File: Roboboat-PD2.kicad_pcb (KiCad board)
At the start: 2 copper layers, 78 x 81.5 mm, 38 parts, among them J1 14.4V, J10 Motor, J11 Motor, J12 Motor, J13 Motor, J14 Motor, J15 Motor, J16 Motor, J17 GND TP, J2 PGOOD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

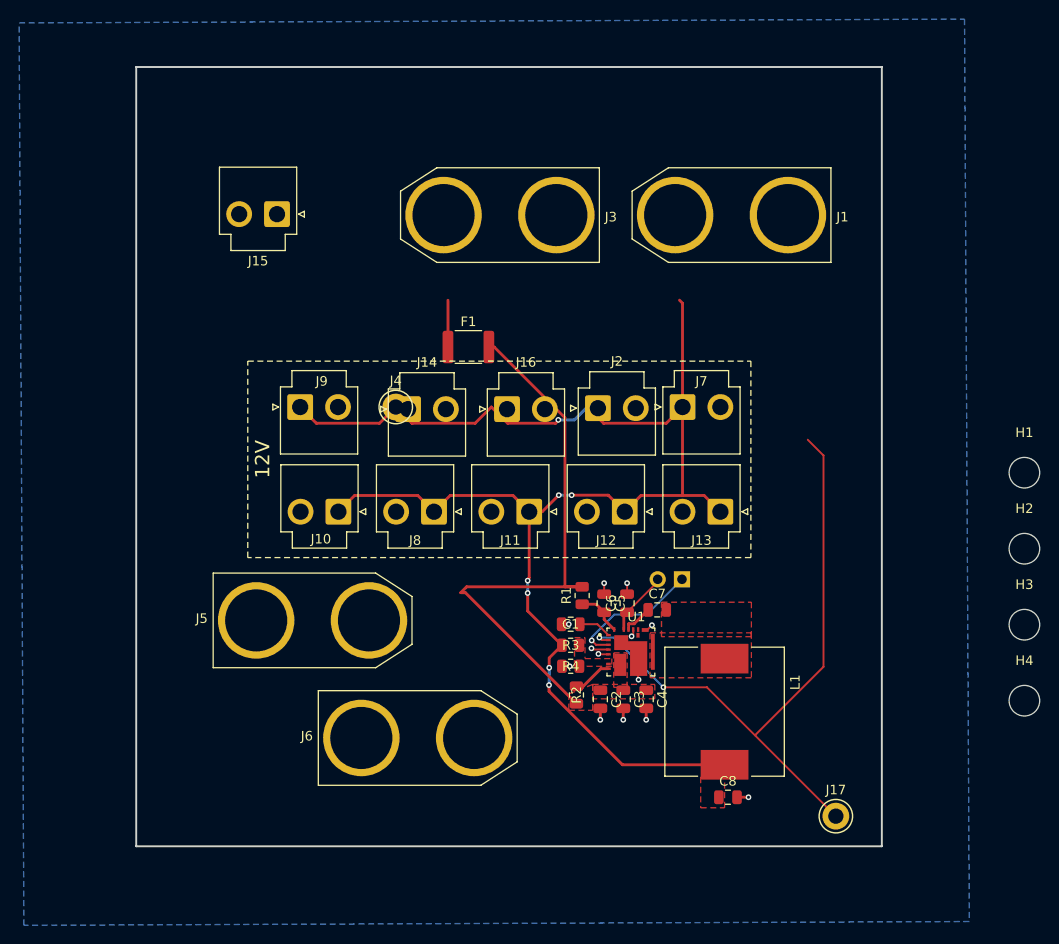
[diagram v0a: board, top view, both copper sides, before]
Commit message: add 0.1uF capacitors to PGOOD output
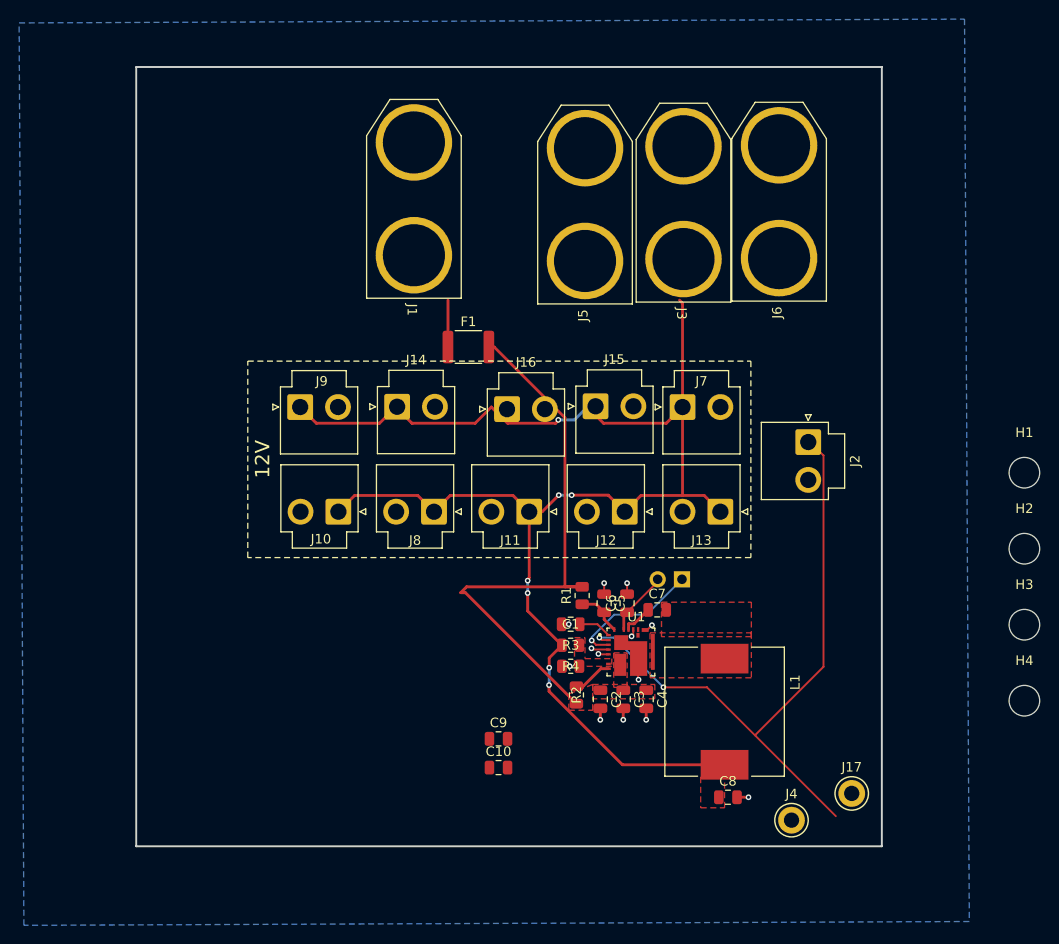
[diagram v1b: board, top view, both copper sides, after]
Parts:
- added C10: 0.1uF, Capacitor_SMD:C_0805_2012Metric, F.Cu at (133.6, 130.7)
- added C9: 0.1uF, Capacitor_SMD:C_0805_2012Metric, F.Cu at (133.6, 127.7)
- moved J6 67.6 mm to (162.9, 71.5), turned to 90 degrees
- moved J4 59.8 mm to (164.2, 136.2)
- moved J5 52.0 mm to (142.6, 71.8), turned to 90 degrees
- moved J15 38.9 mm to (143.7, 92.9), turned to 0 degrees
- moved J1 33.3 mm to (124.7, 71.2), turned to 90 degrees
- moved J2 22.3 mm to (165.9, 96.6), turned to -90 degrees
- moved J3 19.2 mm to (152.9, 71.6), turned to 90 degrees
- moved J17 2.90 mm to (170.5, 133.4)
- moved J14 1.17 mm to (122.9, 93.0)
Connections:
- J17 pad 1: GND -> Net-(J17-Pin_1)
- J2 pad 2: GND -> Net-(J2-Pin_2)

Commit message: add 0.1uF capacitors to PGOOD output
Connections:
- C10 pad 1: Net-(J17-Pin_1) -> /PGOOD
- C9 pad 1: Net-(J2-Pin_2) -> /PGOOD
- J17 pad 1: Net-(J17-Pin_1) -> GND
- J2 pad 2: Net-(J2-Pin_2) -> /PGOOD
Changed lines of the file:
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@@
 	(net 13 "Net-(SW1-A)")
 	(net 14 "Net-(SW1-B)")
-	(net 15 "Net-(J2-Pin_2)")
-	(net 16 "Net-(J17-Pin_1)")
 	(footprint "Capacitor_SMD:C_0805_2012Metric"
 		(layer "F.Cu")
@@
 			(layers "*.Cu" "*.Mask")
 			(remove_unused_layers no)
-			(net 16 "Net-(J17-Pin_1)")
+			(net 1 "GND")
 			(pinfunction "Pin_1")
 			(pintype "passive")
@@
 			(layers "*.Cu" "*.Mask")
 			(remove_unused_layers no)
-			(net 15 "Net-(J2-Pin_2)")
+			(net 3 "/PGOOD")
 			(pinfunction "Pin_2")
 			(pintype "passive")
@@
 			(layers "F.Cu" "F.Paste" "F.Mask")
 			(roundrect_rratio 0.25)
-			(net 15 "Net-(J2-Pin_2)")
+			(net 3 "/PGOOD")
 			(pintype "passive")
 		)
@@
 			(layers "F.Cu" "F.Paste" "F.Mask")
 			(roundrect_rratio 0.25)
-			(net 16 "Net-(J17-Pin_1)")
+			(net 3 "/PGOOD")
 			(pintype "passive")
 		)
@@
 		(tags "connector JST VH vertical")
 		(property "Reference" "J15"
-			(at 1.98 -4.9 360)
+			(at 1.98 -4.9 0)
 			(layer "F.SilkS")
 			(effects
@@
 		)
 		(property "Value" "Motor"
-			(at 1.98 6 360)
+			(at 1.98 6 0)
 			(layer "F.Fab")
 			(effects
@@
 		)
 		(fp_text user "${REFERENCE}"
-			(at 1.98 4.1 360)
+			(at 1.98 4.1 0)
 			(layer "F.Fab")
 			(effects

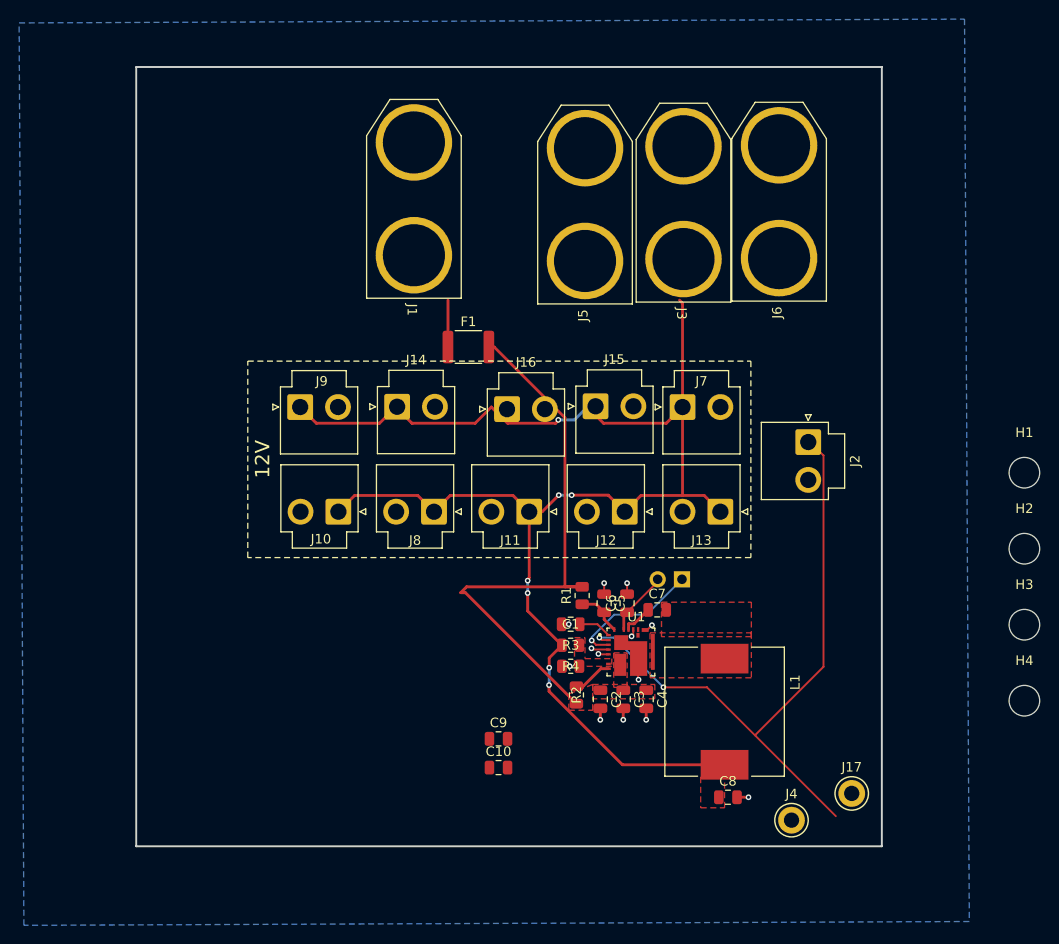
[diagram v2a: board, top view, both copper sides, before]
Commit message: redo PCB layout
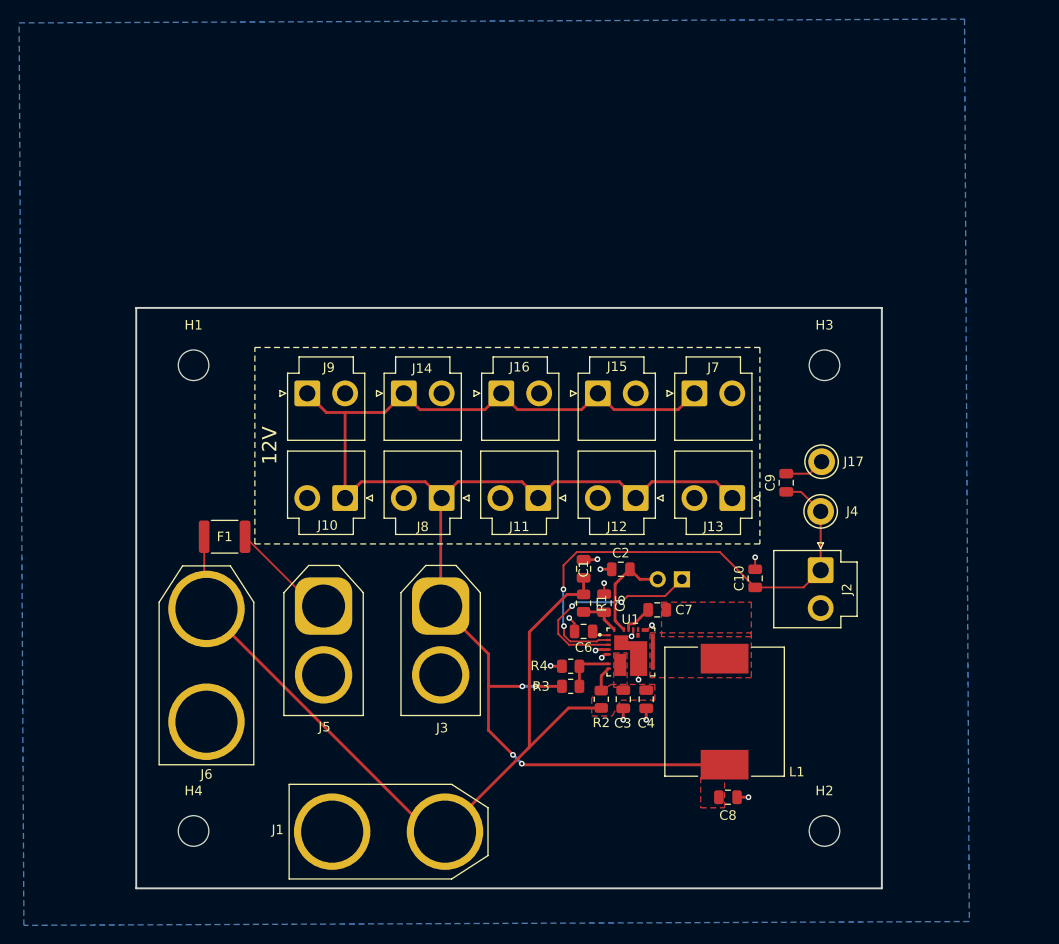
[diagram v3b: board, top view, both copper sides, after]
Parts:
- J3, J5: footprint footprints:XT90_V -> Connector_AMASS:AMASS_XT60-M_1x02_P7.20mm_Vertical
- moved H4 88.0 mm to (101.7, 137.3)
- moved H1 87.6 mm to (101.7, 88.6)
- moved J6 77.1 mm to (103.0, 120.0)
- moved J1 66.3 mm to (122.0, 137.4), turned to 0 degrees
- moved J5 50.1 mm to (115.2, 113.8), turned to -90 degrees
- moved J3 49.3 mm to (127.5, 113.8), turned to -90 degrees
- moved C9 40.3 mm to (163.7, 100.9), turned to 90 degrees
- moved H2 36.2 mm to (167.7, 137.3)
- moved J17 34.8 mm to (167.3, 98.7)
- moved H3 34.3 mm to (167.7, 88.6)
- moved C10 33.4 mm to (160.4, 110.9), turned to 90 degrees
- moved J4 32.4 mm to (167.2, 103.9)
- moved F1 32.3 mm to (104.9, 106.5), turned to 180 degrees
- moved C2 13.8 mm to (146.3, 110.0), turned to 180 degrees
- moved J2 13.5 mm to (167.2, 110.0)
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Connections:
- J2 pad 2: /PGOOD -> GND
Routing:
- net +14.4V: track 60.4 -> 83.2 mm
- net /PGOOD: track 68.1 -> 52.7 mm
- net Net-(SW1-A): track 14.2 -> 21.9 mm, vias 1 -> 2
- net +12V: track 154.3 -> 161.7 mm, vias 7 -> 4
- net GND: track 15.5 -> 21.7 mm, vias 13 -> 14
- net Net-(J5-Pin_1): track 4.89 -> 10.3 mm
- net Net-(U1-FB): track 0.00 -> 4.89 mm
- net Net-(SW1-B): track 5.99 -> 10.7 mm
- net Net-(U1-SS): track 3.48 -> 1.82 mm
- net Net-(U1-TON): track 4.11 -> 2.60 mm
- removed copper zone on F.Cu, net Net-(U1-FB)
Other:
- board size 78 x 81.5 mm -> 78 x 60.7 mm

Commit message: better silkscreens
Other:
- board text added: "14.4V"
- board text added: "14.4V INPUT"
- board text added: "FUSED 14.4V"
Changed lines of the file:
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@@
 		)
 		(property "Footprint" "footprints:XT90_V"
-			(at 0 0 360)
+			(at 0 0 0)
 			(layer "F.Fab")
 			(hide yes)
@@
 		)
 		(property "Datasheet" ""
-			(at 0 0 360)
+			(at 0 0 0)
 			(layer "F.Fab")
 			(hide yes)
@@
 		)
 		(property "Description" "Generic connector, single row, 01x02, script generated (kicad-library-utils/schlib/autogen/connector/)"
-			(at 0 0 360)
+			(at 0 0 0)
 			(layer "F.Fab")
 			(hide yes)
@@
 		(tags "XT60 female vertical")
 		(property "Reference" "J3"
-			(at 12.75 -0.15 180)
+			(at 11.2 -0.15 180)
 			(layer "F.SilkS")
 			(effects
@@
 		(tags "capacitor")
 		(property "Reference" "C6"
-			(at 0 -1.68 360)
+			(at 0 -1.68 0)
 			(layer "F.SilkS")
 			(effects
@@
 		)
 		(property "Value" "10nF"
-			(at 0 1.68 360)
+			(at 0 1.68 0)
 			(layer "F.Fab")
 			(effects
@@
 		)
 		(fp_text user "${REFERENCE}"
-			(at 0 0 360)
+			(at 0 0 0)
 			(layer "F.Fab")
 			(effects
@@
 		(tags "capacitor")
 		(property "Reference" "C1"
-			(at 0 0 90)
+			(at 0 -1.65 90)
 			(layer "F.SilkS")
 			(effects
@@
 		(tags "XT60 female vertical")
 		(property "Reference" "J5"
-			(at 12.65 -0.1 0)
+			(at 10.95 -0.05 0)
 			(layer "F.SilkS")
 			(effects
@@
 		(tags "capacitor")
 		(property "Reference" "C2"
-			(at 0 1.7 360)
+			(at 0 1.7 0)
 			(layer "F.SilkS")
 			(effects
@@
 		)
 		(property "Value" "4.7uF"
-			(at 0 1.68 360)
+			(at 0 1.68 0)
 			(layer "F.Fab")
 			(effects
@@
 		)
 		(fp_text user "${REFERENCE}"
-			(at 0 0 360)
+			(at 0 0 0)
 			(layer "F.Fab")
 			(effects
@@
 		(tags "resistor")
 		(property "Reference" "R1"
-			(at 0 1.9 90)
+			(at 0 -1.65 90)
 			(layer "F.SilkS")
 			(effects
@@
 		(tags "fuse")
 		(property "Reference" "F1"
-			(at 0 0 360)
+			(at 0 0 0)
 			(layer "F.SilkS")
 			(effects
@@
 		)
 		(property "Value" "Fuse"
-			(at 0 2.65 360)
+			(at 0 2.65 0)
 			(layer "F.Fab")
 			(effects
@@
 		)
 		(fp_text user "${REFERENCE}"
-			(at 0 0 360)
+			(at 0 0 0)
 			(layer "F.Fab")
 			(effects
@@
 		)
 	)
+	(gr_text "FUSED\n14.4V"
+		(at 111.7 130 0)
+		(layer "F.SilkS")
+		(effects
+			(font
+				(size 1.5 1.5)
+				(thickness 0.15)
+			)
+			(justify left bottom)
+		)
+	)
 	(gr_text "12V"
 		(at 110.4925 99.02 90)
 		(layer "F.SilkS")
 		(effects
+			(font
+				(size 1.5 1.5)
+				(thickness 0.15)
+			)
+			(justify left bottom)
+		)
+	)
+	(gr_text "14.4V\nINPUT"
+		(at 133.2 139.3 0)
+		(layer "F.SilkS")
+		(effects
+			(font
+				(size 1.5 1.5)
+				(thickness 0.15)
+			)
+			(justify left bottom)
+		)
+	)
+	(gr_text "12V"
+		(at 125.65 127.55 0)
+		(layer "F.SilkS")
+		(effects
+			(font
+				(size 1.5 1.5)
+				(thickness 0.15)
+			)
+			(justify left bottom)
+		)
+	)
+	(gr_text "14.4V"
+		(at 109.95 123.6 90)
+		(layer "F.SilkS")
+		(effects
